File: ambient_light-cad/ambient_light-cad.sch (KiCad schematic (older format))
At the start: 31 parts, among them U1 ATmega328P-AU

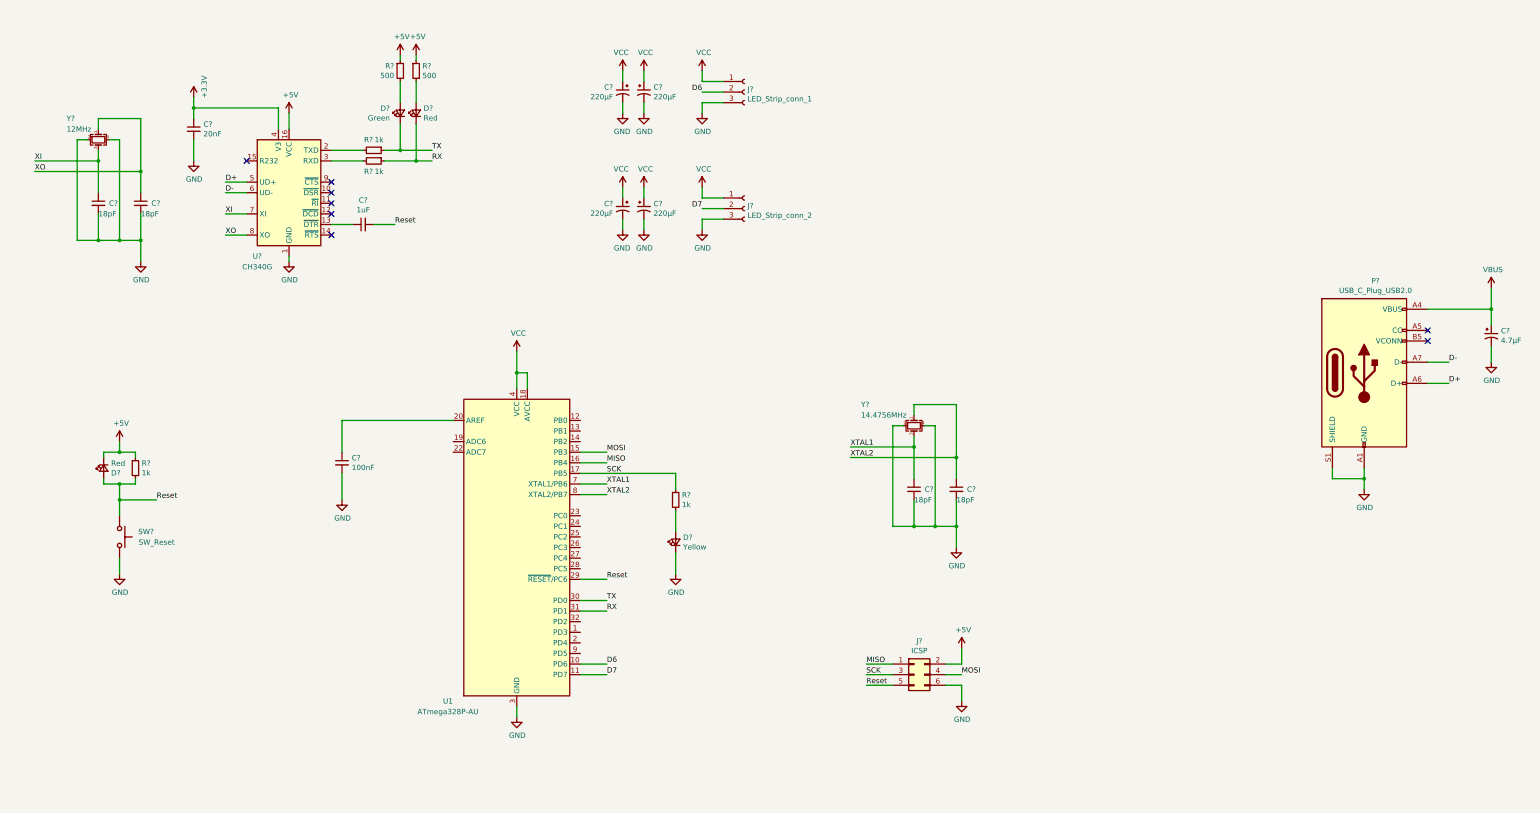
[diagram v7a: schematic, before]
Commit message: [Modified] Schematic size A3 to A4
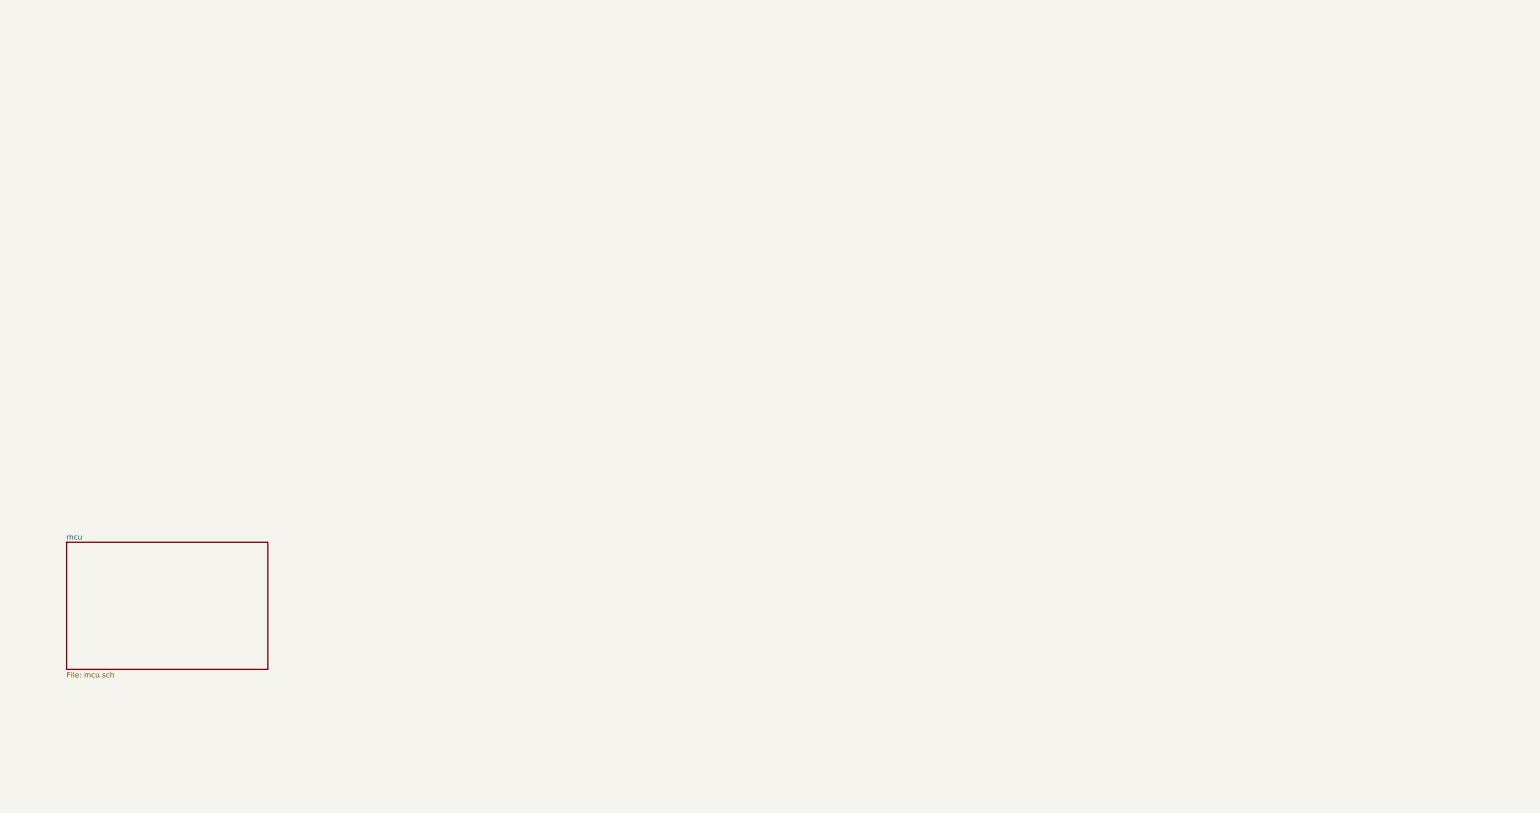
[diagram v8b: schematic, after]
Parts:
- removed C?: 100nF, symbol Device:C_Small
- removed C? (x4): 18pF, symbol Device:C_Small
- removed C?: 20nF, symbol Device:C_Small
- removed C?: 1uF, symbol Device:C_Small
- removed C?: 4.7μF, symbol Device:CP1_Small
- removed C? (x4): 220μF, symbol Device:CP1_Small
- removed D?: Green, symbol Device:LED_Small
- removed D?: Yellow, symbol Device:LED_Small
- removed D? (x2): Red, symbol Device:LED_Small
- removed J?: ICSP, symbol Connector_Generic:Conn_02x03_Odd_Even
- removed J?: LED_Strip_conn_1, symbol Connector:Conn_01x03_Female
- removed J?: LED_Strip_conn_2, symbol Connector:Conn_01x03_Female
- removed P?: USB_C_Plug_USB2.0, symbol ambient_light-cad-rescue:USB_C_Plug_USB2.0-Connector
- removed R? (x4): 1k, symbol Device:R_Small
- removed R? (x2): 500, symbol Device:R_Small
- removed SW?: SW_Reset, symbol Switch:SW_Push
- removed U1: ATmega328P-AU, Package_QFP:TQFP-32_7x7mm_P0.8mm, symbol MCU_Microchip_ATmega:ATmega328P-AU
- removed U?: CH340G, Package_SO:SOIC-16_3.9x9.9mm_P1.27mm, symbol Interface_USB:CH340G
- removed Y?: 14.4756MHz, symbol Device:Crystal_GND24_Small
- removed Y?: 12MHz, symbol Device:Crystal_GND24_Small
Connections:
- no-connect marks 8 -> 0
